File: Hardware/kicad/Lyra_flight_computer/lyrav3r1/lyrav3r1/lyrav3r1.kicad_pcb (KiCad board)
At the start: 4 copper layers, 25 x 55 mm, 76 parts, among them J1 Conn_01x02, J2 Screw_Terminal_01x06, J3 Conn_01x02, J4 Conn_01x02, J6 Conn_01x06, J7 USB_B_Micro, J8 Conn_01x04, J9 Screw_Terminal_01x06, Q1 AO3401A, Q2 AO3400A, Q3 AO3400A, Q4 AO3400A, Q5 AO3400A, U2 BMI088, U3 BMP388, U4 ADXL375BCCZ-RL7, U5 AMS1117-3.3, U8 RP2040, U9 W25Q128JVS, X2 SX1M12.000M10F30TNN

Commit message: stuffs
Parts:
- removed D4: LED_ARGB, customfootprints:LED_Cree-PLCC4_2x2mm_CCW
- removed LS1: PKMCS0909E4000-R1, SamacSys_Parts4:PKMCS0909E4000R1
- added REF**: ublox_SAM-M8Q, RF_GPS:ublox_SAM-M8Q, F.Cu at (196.1, 78.6)
- added U6: SX1262IMLTRT, easyeda2kicad:QFN-24_L4.0-W4.0-P0.50-BL-EP2.6, B.Cu at (192.2, 73.2)
- C9, D2, J1, J6, J8: moved to B.Cu
- moved C5 94.2 mm to (123.3, 65.5), turned to 180 degrees
- moved C6 90.0 mm to (123.3, 68.0), turned to 180 degrees
- moved U9 82.3 mm to (128.1, 60.9), turned to 180 degrees
- moved J4 79.8 mm to (123.4, 92.7), turned to 180 degrees
- moved J8 79.6 mm to (127.9, 86.2), turned to 180 degrees
- moved C27 78.6 mm to (129.5, 82.9), turned to 180 degrees
- moved C7 76.1 mm to (123.3, 70.5), turned to 180 degrees
- moved J3 74.9 mm to (123.4, 89.2), turned to 180 degrees
- moved J7 71.5 mm to (138.1, 60.2), turned to 180 degrees
- moved U3 70.4 mm to (124.0, 96.1)
- moved C25 70.4 mm to (129.5, 78.9), turned to 180 degrees
- moved D2 69.6 mm to (132.6, 94.7), turned to 180 degrees
- moved D1 69.5 mm to (125.1, 81.6), turned to 180 degrees
- moved C17 68.3 mm to (132.4, 75.0), turned to 180 degrees
- moved C18 67.5 mm to (132.4, 77.0), turned to 180 degrees
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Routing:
- net +12P: track 95.1 -> 0.00 mm
- net GND: track 59.6 -> 0.00 mm, vias 36 -> 0
- net +3V3: track 47.1 -> 0.00 mm, vias 20 -> 0
- net /QSPI_SS: track 44.5 -> 0.00 mm, vias 4 -> 0
- net /RUN: track 28.0 -> 0.00 mm, vias 2 -> 0
- net /P1 CONT : track 27.2 -> 0.00 mm
- net VBUS: track 26.8 -> 0.00 mm, vias 2 -> 0
- net /I2C1 SCL: track 25.7 -> 0.00 mm, vias 4 -> 0
- net /I2C1 SDA: track 23.8 -> 0.00 mm
- net /P1 EN : track 22.7 -> 0.00 mm
- net /P2 CONT : track 20.3 -> 0.00 mm
- net /BRKOUT1: track 18.9 -> 0.00 mm
- net /P4 CONT : track 16.0 -> 0.00 mm
- net /P2 EN : track 15.7 -> 0.00 mm
- net /BRKOUT2: track 15.6 -> 0.00 mm
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- removed copper zone on F.Cu, net +1V1
- removed copper zone on B.Cu, net +3V3
- removed copper zone on B.Cu, net GND
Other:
- board text removed: "+"
- board text removed: "-"
- board text removed: "BATT+"
- board text removed: "BATT-"
- board text removed: "BOOT"
- board text removed: "CLK"
- board text removed: "JLCJLCJLCJLC"
- board text removed: "LYRA"
- board text removed: "P1+"
- board text removed: "P1-"
- board text removed: "P2+"
- board text removed: "P2-"
- board text removed: "P3+"
- board text removed: "P3-"
- board text removed: "P4+"
- board text removed: "P4-"
- board text removed: "PRS"
- board text removed: "RST"
- board text removed: "SW+"
- board text removed: "SW-"
- board text removed: "V3"

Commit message: gps thingings
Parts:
- removed J8: Conn_01x04, Connector_PinHeader_2.54mm:PinHeader_1x04_P2.54mm_Vertical
- removed REF**: ublox_SAM-M8Q, RF_GPS:ublox_SAM-M8Q
- added R8: 100, Resistor_SMD:R_0402_1005Metric, F.Cu at (172.4, 81.1)
- added U1: 0900FM15D0039E, footprints:0900FM15D0039E_JOT, B.Cu at (196.7, 72.3)
- J6: value Conn_01x06 -> Conn_Coaxial; footprint Connector_PinHeader_2.54mm:PinHeader_1x06_P2.54mm_Vertical -> Connector_Coaxial:SMA_Amphenol_132289_EdgeMount; moved to F.Cu
- moved J6 54.9 mm to (195.9, 66.6), turned to 90 degrees
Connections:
- J6 pad 1: /BRKOUT7 -> unconnected-(J6-In-Pad1)
- J6 pad 2: /BRKOUT6 -> unconnected-(J6-Ext-Pad2)
- Q4 pad 1: /P3 EN  -> Net-(Q4-G)
- R17 pad 2: /P3 EN  -> Net-(Q4-G)

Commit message: more radio stuffs
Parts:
- removed U1: 0900FM15D0039E, footprints:0900FM15D0039E_JOT
- added U7: LIS3MDL, Package_LGA:LGA-12_2x2mm_P0.5mm, F.Cu at (139.6, 74.1)
- C1, C10, C11, C12, C13, C16, C17, C18, C19, C2, C21, C22, C23, C24, C25, C26, C27, C3, C4, C5, C6, C7, C8, C9, D1, D2, J1, J3, J4, J7, Q1, Q2, Q3, Q4, Q5, R1, R10, R11, R12, R13, R14, R15, R16, R17, R18, R2, R21, R22, R23, R24, R25, R26, R27, R28, R3, R4, R5, R6, R7, U2, U3, U4, U5, U6, U8, U9, X2: moved to F.Cu
- moved J2 89.7 mm to (116.5, 64.0), turned to 0 degrees
- moved J9 80.1 mm to (116.5, 72.3), turned to 0 degrees
- moved U5 61.9 mm to (144.8, 80.6), turned to 0 degrees
- moved U8 60.5 mm to (135.2, 81.1), turned to 0 degrees
- moved J6 59.9 mm to (136.0, 66.0), turned to 0 degrees
- moved R8 49.3 mm to (123.2, 77.4)
- moved Q5 42.0 mm to (116.4, 97.3), turned to 0 degrees
- moved Q4 42.0 mm to (116.4, 92.7), turned to 0 degrees
- moved Q3 41.9 mm to (116.4, 88.1), turned to 0 degrees
- moved Q2 41.9 mm to (116.4, 83.4), turned to 0 degrees
- moved Q1 41.9 mm to (116.4, 78.8), turned to 0 degrees
- moved U3 41.9 mm to (165.6, 92.0), turned to 0 degrees
- moved U6 38.9 mm to (156.6, 89.1), turned to 0 degrees
- moved R1 34.1 mm to (120.3, 77.4), turned to 0 degrees
- moved R2 34.1 mm to (120.3, 79.4), turned to 0 degrees
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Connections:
- U6 pad 2: unconnected-(U6-GND-Pad2) -> GND
- U6 pad 20: unconnected-(U6-GND-Pad20) -> GND
- U6 pad 21: unconnected-(U6-RFI_P-Pad21) -> Net-(U1-RFI_P)
- U6 pad 22: unconnected-(U6-RFI_N-Pad22) -> Net-(U1-RFI_N)
- U6 pad 23: unconnected-(U6-RFO-Pad23) -> Net-(U1-RFO)
- U6 pad 25: unconnected-(U6-GND-Pad25) -> GND
- U6 pad 5: unconnected-(U6-GND-Pad5) -> GND
- U6 pad 8: unconnected-(U6-GND-Pad8) -> GND

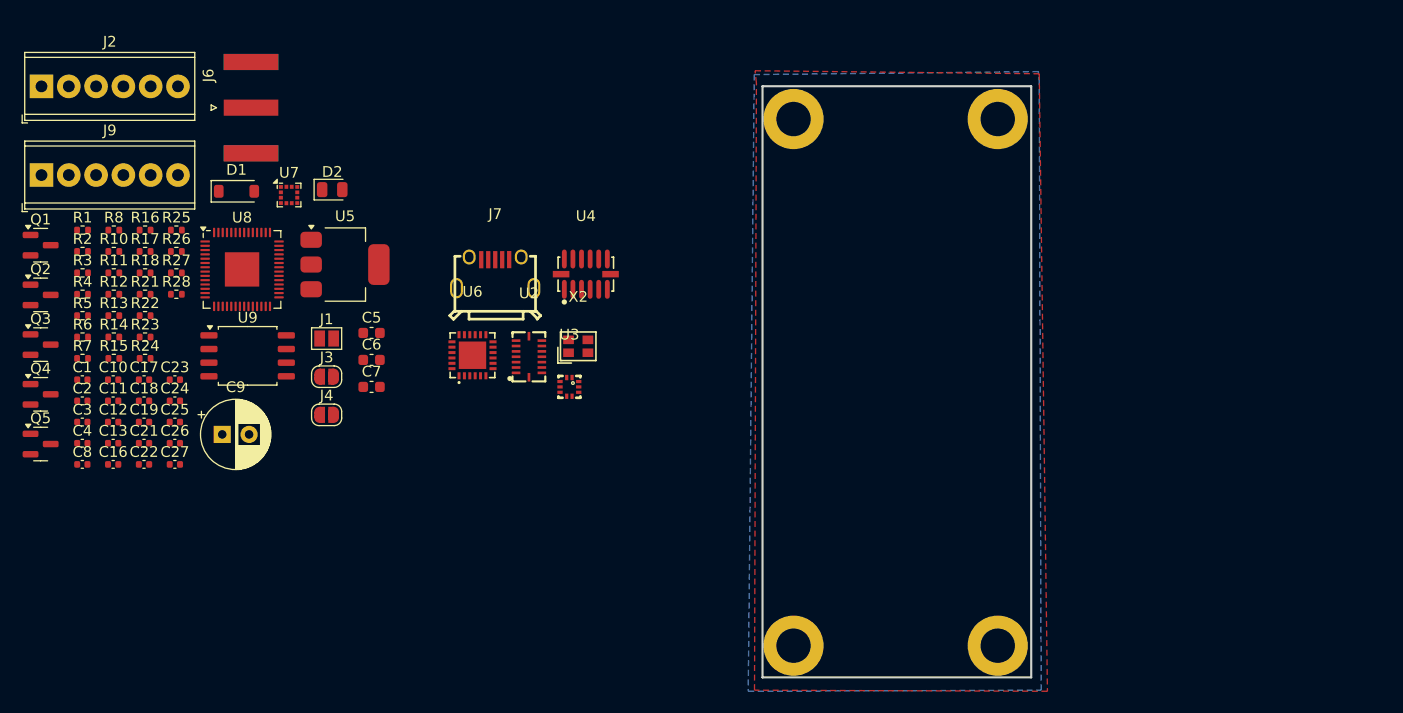
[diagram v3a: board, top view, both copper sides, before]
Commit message: gps init, moar librarys
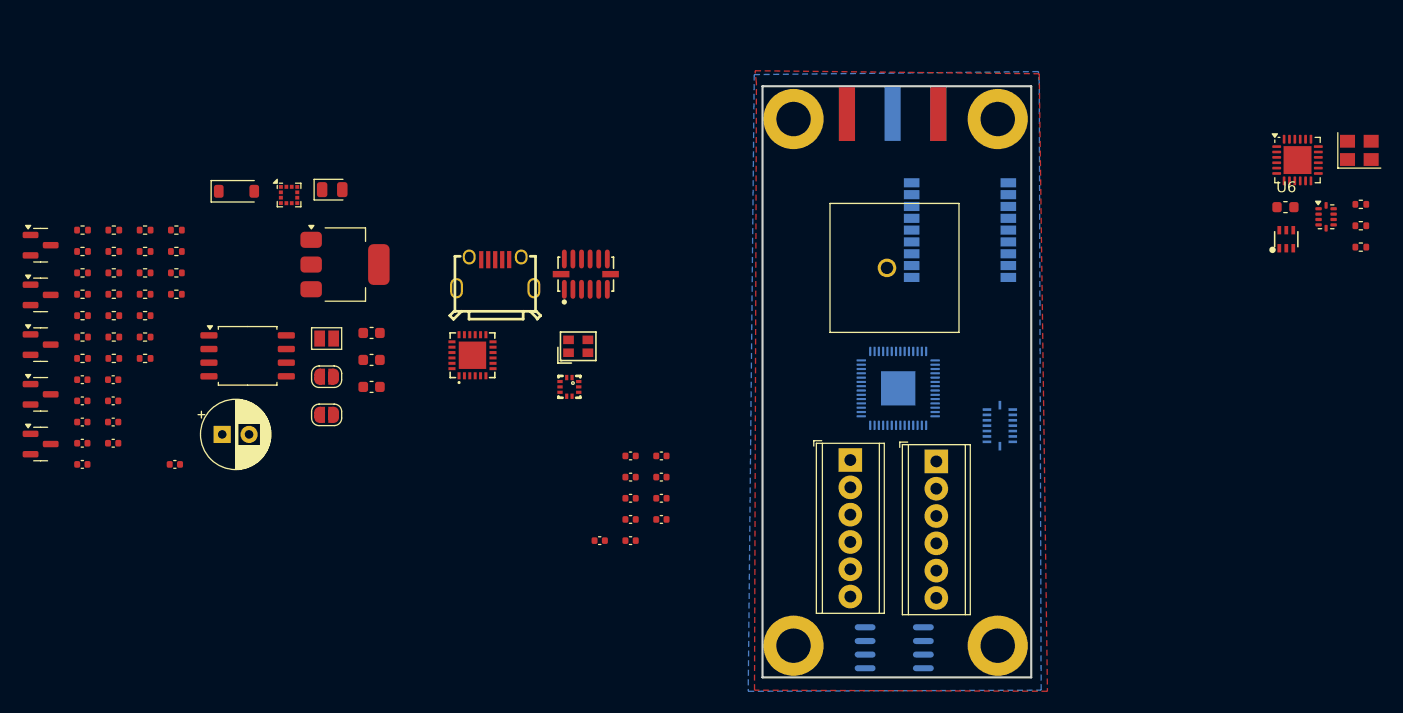
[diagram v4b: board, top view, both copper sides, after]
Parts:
- added AE1: Antenna, SamacSys_Parts:GP1575124A02, F.Cu at (195.2, 80.9)
- added FL1: 0900FM15K0039, RF_Converter:Balun_Johanson_0900FM15K0039, F.Cu at (236.0, 76.2)
- added IC1: TESEO-LIV3F, SamacSys_Parts:SON110P970X1010X230-18N, B.Cu at (202.0, 77.4)
- added L2: 15uH, Inductor_SMD:L_0603_1608Metric, F.Cu at (232.3, 75.3)
- added R19: 100, Resistor_SMD:R_0402_1005Metric, F.Cu at (239.3, 79.0)
- added R6: 5.1k, Resistor_SMD:R_0402_1005Metric, F.Cu at (239.3, 75.0)
- added R7: 100, Resistor_SMD:R_0402_1005Metric, F.Cu at (239.3, 77.0)
- added U1: SX1262IMLTRT, Package_DFN_QFN:QFN-24-1EP_4x4mm_P0.5mm_EP2.6x2.6mm, F.Cu at (233.4, 70.9)
- added U6: PE4259-63, .pretty:SC-70-6_L2.2-W1.3-P0.65-LS2.1-BL, F.Cu at (232.3, 78.3)
- added U7: TPS54331DR, .pretty:SOIC-8_L5.0-W4.0-P1.27-LS6.0-BL, B.Cu at (195.9, 116.3)
- added Y1: CF4032M00012001, Crystal:Crystal_SMD_3225-4Pin_3.2x2.5mm, F.Cu at (239.1, 70.0)
- J6, U2, U8: moved to B.Cu
- moved J9 87.4 mm to (199.8, 98.9), turned to -90 degrees
- moved J2 82.9 mm to (191.8, 98.8), turned to -90 degrees
- moved U8 62.0 mm to (196.2, 92.1), turned to 180 degrees
- moved J6 59.7 mm to (195.7, 66.6), turned to 90 degrees
- moved C16 45.8 mm to (168.5, 106.3)
- moved C17 45.8 mm to (171.3, 98.4)
- moved C18 45.8 mm to (171.3, 100.4)
- moved C19 45.8 mm to (171.3, 102.4)
- moved C21 45.8 mm to (171.3, 104.3)
- moved C22 45.8 mm to (171.3, 106.3)
- moved C23 45.8 mm to (174.2, 98.4)
- moved C24 45.8 mm to (174.2, 100.4)
- moved C25 45.8 mm to (174.2, 102.4)
- moved C26 45.8 mm to (174.2, 104.3)
- moved U2 44.3 mm to (205.7, 95.6), turned to 180 degrees
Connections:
- J6 pad 1: unconnected-(J6-In-Pad1) -> Net-(J6-In)
- J6 pad 2: unconnected-(J6-Ext-Pad2) -> GND
- U2 pad 10: GND -> unconnected-(U2-SDO2-Pad10)
- U2 pad 14: +3V3 -> unconnected-(U2-CSB1-Pad14)
- U2 pad 15: GND -> unconnected-(U2-SDO1-Pad15)
- U2 pad 7: +3V3 -> unconnected-(U2-PS-Pad7)
- U2 pad 8: /I2C1 SCL -> unconnected-(U2-SCL/SCK-Pad8)
- U2 pad 9: /I2C1 SDA -> unconnected-(U2-SDA/SDI-Pad9)
- U3 pad 2: /I2C1 SCL -> unconnected-(U3-SCK-Pad2)
- U3 pad 4: /I2C1 SDA -> unconnected-(U3-SDI-Pad4)
- U3 pad 5: GND -> unconnected-(U3-SDO-Pad5)
- U3 pad 6: +3V3 -> unconnected-(U3-CSB-Pad6)
- U4 pad 13: /I2C1 SDA -> unconnected-(U4-SDA/SDI/SDIO-Pad13)
- U4 pad 14: /I2C1 SCL -> unconnected-(U4-SCL/SCLK-Pad14)
- U8 pad 27: /BRKOUT5 -> unconnected-(U8-GPIO16-Pad27)
- U8 pad 28: /BRKOUT6 -> unconnected-(U8-GPIO17-Pad28)
- U8 pad 29: /BRKOUT7 -> unconnected-(U8-GPIO18-Pad29)
- U8 pad 34: /I2C1 SDA -> unconnected-(U8-GPIO22-Pad34)
- U8 pad 35: /I2C1 SCL -> unconnected-(U8-GPIO23-Pad35)

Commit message: gps and rf
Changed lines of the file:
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@@
 		(fp_arc
 			(start -2.5 0.73)
-			(mid -2.50637 -0.729972)
+			(mid -2.50635 -0.729972)
 			(end -2.48726 0.729889)
 			(stroke
@@
 	)
 	(gr_rect
+		(start 214.1832 78.298)
+		(end 228.1832 98.298)
+		(stroke
+			(width 0.2)
+			(type default)
+		)
+		(fill none)
+		(layer "F.Cu")
+	)
+	(gr_rect
